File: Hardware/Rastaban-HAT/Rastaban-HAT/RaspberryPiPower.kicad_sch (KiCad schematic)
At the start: 13 parts, among them IC2 BCM53DS, Q3 DMG2305UX-7, U5 LM2596S-ADJ

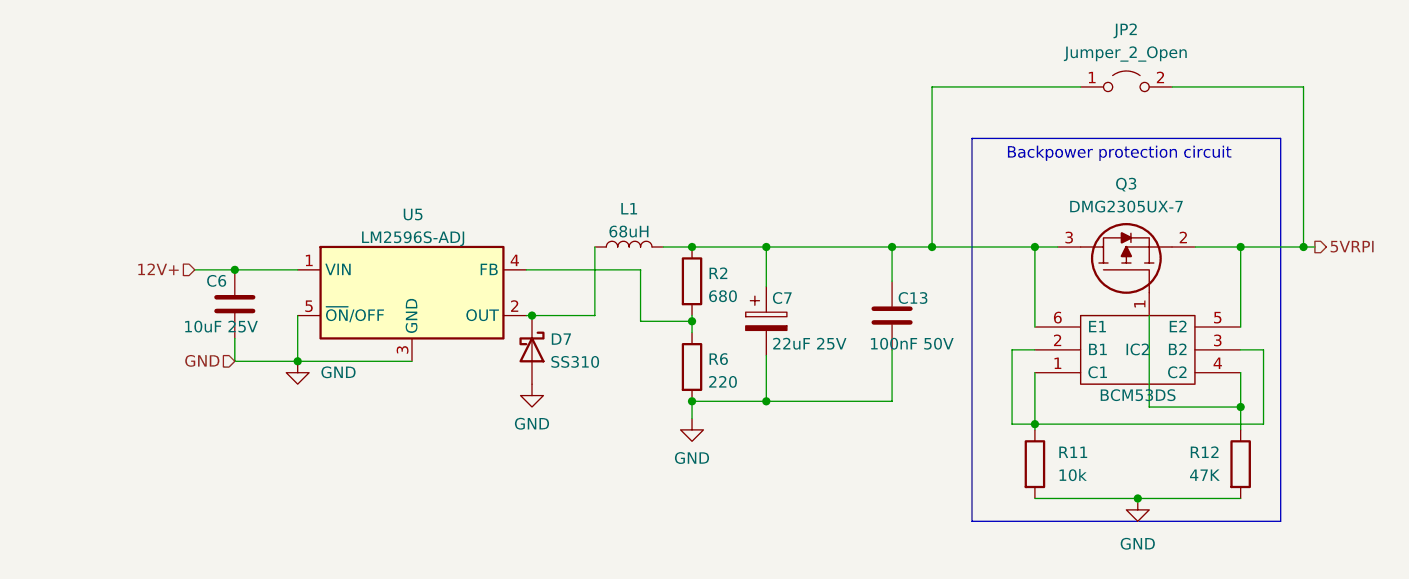
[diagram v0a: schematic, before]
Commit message: changed jumpers to 3.3V jumpers only
changed version numbers
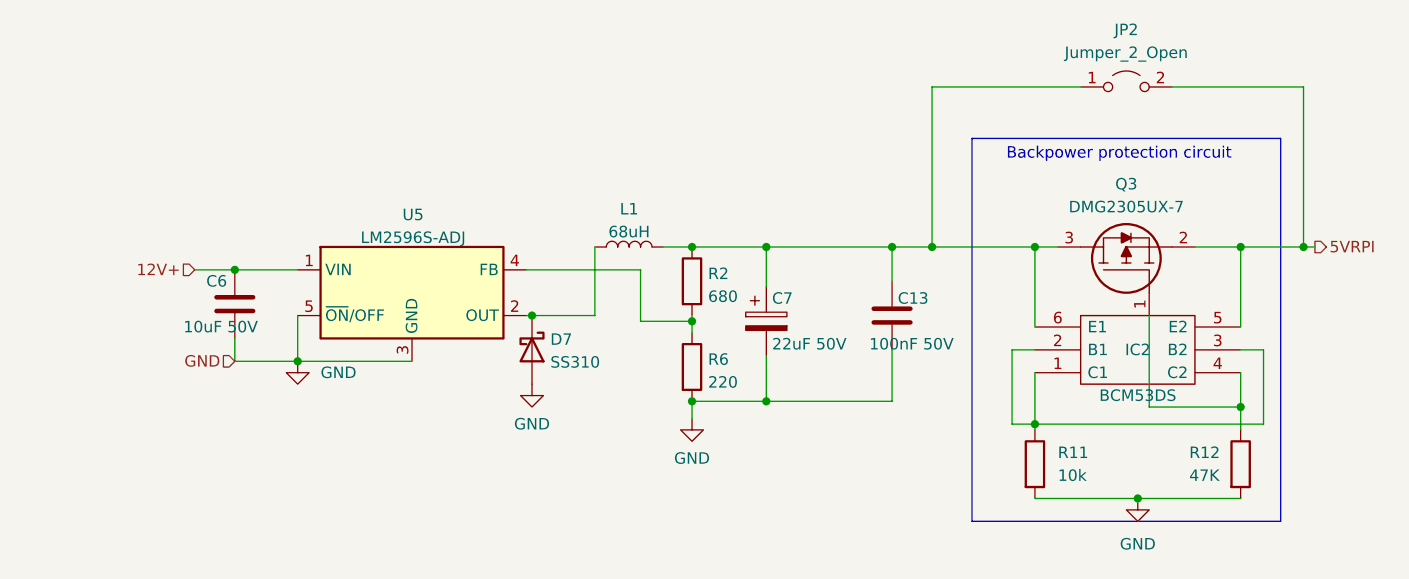
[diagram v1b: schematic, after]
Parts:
- C6: value 10uF 25V -> 10uF 50V
- C7: value 22uF 25V -> 22uF 50V
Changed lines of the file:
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@@
       (effects (font (size 1.27 1.27)) (justify left))
     )
-    (property "Value" "22uF 25V" (id 1) (at 109.855 69.215 0)
+    (property "Value" "22uF 50V" (id 1) (at 109.855 69.215 0)
       (effects (font (size 1.27 1.27)) (justify left))
     )
@@
       (effects (font (size 1.27 1.27)) (justify left))
     )
-    (property "Value" "10uF 25V" (id 1) (at 44.45 67.31 0)
+    (property "Value" "10uF 50V" (id 1) (at 44.45 67.31 0)
       (effects (font (size 1.27 1.27)) (justify left))
     )

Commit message: changed some component values in RPI power circuit
New components
-lm2596s -5.0
-ss510
Removed:
feedback resistors
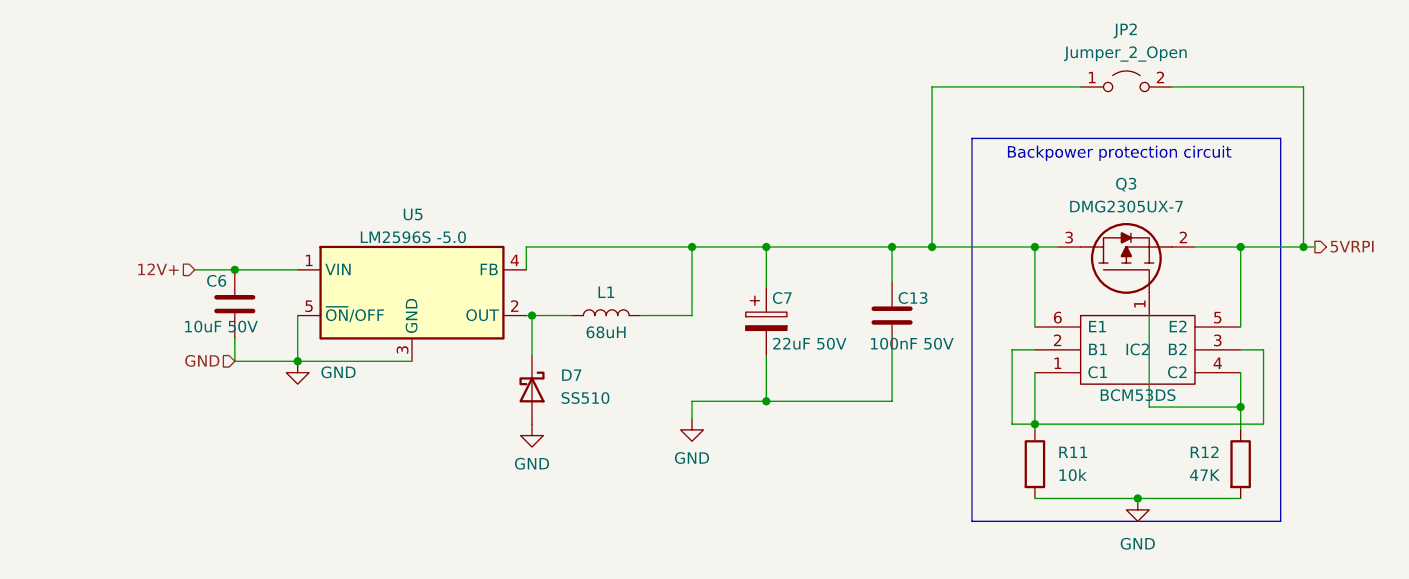
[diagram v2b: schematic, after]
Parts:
- removed R2: 680, Resistor_SMD:R_0805_2012Metric_Pad1.20x1.40mm_HandSolder, symbol Device:R
- removed R6: 220, Resistor_SMD:R_0805_2012Metric_Pad1.20x1.40mm_HandSolder, symbol Device:R
- D7: value SS310 -> SS510
- JP2: Purpose (none) -> Bypass Backpower protection circuit
- U5: value LM2596S-ADJ -> LM2596S -5.0; LCSC C347423 -> (none)
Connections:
- net at C13.2, C7.1, IC2.6 (E1)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: now also U5.4 (FB)
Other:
- moved on the sheet: D7, L1
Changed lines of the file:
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@@
   (title_block
     (title "Rastaban-HAT")
-    (date "2022-11-21")
-    (rev "1.4")
+    (date "2022-12-08")
+    (rev "1.5")
     (company "HAN")
     (comment 1 "Casper R. Tak")
@@
   (junction (at 50.165 60.96) (diameter 0) (color 0 0 0 0)
   )
+  (junction (at 100.965 58.42) (diameter 0) (color 0 0 0 0)
+  )
   (junction (at 139.065 58.42) (diameter 0) (color 0 0 0 0)
   )
-  (junction (at 100.965 75.565) (diameter 0) (color 0 0 0 0)
-  )
   (junction (at 161.925 58.42) (diameter 0) (color 0 0 0 0)
   )
@@
   (junction (at 139.065 78.105) (diameter 0) (color 0 0 0 0)
   )
-  (junction (at 100.965 58.42) (diameter 0) (color 0 0 0 0)
-  )
   (junction (at 127.635 58.42) (diameter 0) (color 0 0 0 0)
   )
-  (junction (at 100.965 66.675) (diameter 0) (color 0 0 0 0)
-  )
   (junction (at 83.185 66.04) (diameter 0) (color 0 0 0 0)
   )
@@
     (stroke (width 0) (type default) (color 0 0 0 0))
   )
+  (wire (pts (xy 83.185 70.485) (xy 83.185 66.04))
+    (stroke (width 0) (type default) (color 0 0 0 0))
+  )
   (wire (pts (xy 50.165 68.58) (xy 50.165 71.12))
     (stroke (width 0) (type default) (color 0 0 0 0))
@@
     (stroke (width 0) (type default) (color 0 0 0 0))
   )
-  (wire (pts (xy 97.79 58.42) (xy 100.965 58.42))
-    (stroke (width 0) (type default) (color 0 0 0 0))
-  )
   (wire (pts (xy 100.965 75.565) (xy 109.22 75.565))
     (stroke (width 0) (type default) (color 0 0 0 0))
   )
-  (wire (pts (xy 95.25 60.96) (xy 95.25 66.675))
+  (wire (pts (xy 82.55 58.42) (xy 100.965 58.42))
     (stroke (width 0) (type default) (color 0 0 0 0))
   )
@@
     (stroke (width 0) (type default) (color 0 0 0 0))
   )
-  (wire (pts (xy 82.55 60.96) (xy 95.25 60.96))
-    (stroke (width 0) (type default) (color 0 0 0 0))
-  )
   (wire (pts (xy 156.845 58.42) (xy 161.925 58.42))
     (stroke (width 0) (type default) (color 0 0 0 0))
@@
     (stroke (width 0) (type default) (color 0 0 0 0))
   )
-  (wire (pts (xy 90.17 66.04) (xy 90.17 58.42))
-    (stroke (width 0) (type default) (color 0 0 0 0))
-  )
   (wire (pts (xy 123.19 58.42) (xy 127.635 58.42))
     (stroke (width 0) (type default) (color 0 0 0 0))
@@
     (stroke (width 0) (type default) (color 0 0 0 0))
   )
-  (wire (pts (xy 100.965 66.675) (xy 100.965 67.945))
-    (stroke (width 0) (type default) (color 0 0 0 0))
-  )
   (wire (pts (xy 139.065 69.85) (xy 136.525 69.85))
     (stroke (width 0) (type default) (color 0 0 0 0))
@@
     (stroke (width 0) (type default) (color 0 0 0 0))
   )
+  (wire (pts (xy 95.25 66.04) (xy 100.965 66.04))
+    (stroke (width 0) (type default) (color 0 0 0 0))
+  )
   (wire (pts (xy 154.305 40.64) (xy 168.91 40.64))
     (stroke (width 0) (type default) (color 0 0 0 0))
@@
     (stroke (width 0) (type default) (color 0 0 0 0))
   )
-  (wire (pts (xy 100.965 66.04) (xy 100.965 66.675))
+  (wire (pts (xy 100.965 58.42) (xy 100.965 66.04))
     (stroke (width 0) (type default) (color 0 0 0 0))
   )
@@
     (stroke (width 0) (type default) (color 0 0 0 0))
   )
+  (wire (pts (xy 82.55 58.42) (xy 82.55 60.96))
+    (stroke (width 0) (type default) (color 0 0 0 0))
+  )
   (wire (pts (xy 161.925 72.39) (xy 161.925 76.2))
     (stroke (width 0) (type default) (color 0 0 0 0))
@@
     (stroke (width 0) (type default) (color 0 0 0 0))
   )
-  (wire (pts (xy 95.25 66.675) (xy 100.965 66.675))
-    (stroke (width 0) (type default) (color 0 0 0 0))
-  )
   (wire (pts (xy 139.065 58.42) (xy 141.605 58.42))
     (stroke (width 0) (type default) (color 0 0 0 0))
@@
     (stroke (width 0) (type default) (color 0 0 0 0))
   )
-  (wire (pts (xy 83.185 66.04) (xy 90.17 66.04))
+  (wire (pts (xy 83.185 66.04) (xy 87.63 66.04))
     (stroke (width 0) (type default) (color 0 0 0 0))
   )
@@
     (pin "2")
   )
-  (symbol (lib_id "power:GND") (at 83.185 73.66 0) (unit 1)
-    (in_bom yes) (on_board yes) (fields_autoplaced)
-    (property "Reference" "#PWR0105" (id 0) (at 83.185 80.01 0)
-      (effects (font (size 1.27 1.27)) hide)
-    )
-    (property "Value" "GND" (id 1) (at 83.185 78.1034 0))
-    (property "Footprint" "" (id 2) (at 83.185 73.66 0)
-      (effects (font (size 1.27 1.27)) hide)
-    )
-    (property "Datasheet" "" (id 3) (at 83.185 73.66 0)
+  (symbol (lib_id "power:GND") (at 83.185 78.105 0) (unit 1)
+    (in_bom yes) (on_board yes) (fields_autoplaced)
+    (property "Reference" "#PWR0105" (id 0) (at 83.185 84.455 0)
+      (effects (font (size 1.27 1.27)) hide)
+    )
+    (property "Value" "GND" (id 1) (at 83.185 82.5484 0))
+    (property "Footprint" "" (id 2) (at 83.185 78.105 0)
+      (effects (font (size 1.27 1.27)) hide)
+    )
+    (property "Datasheet" "" (id 3) (at 83.185 78.105 0)
       (effects (font (size 1.27 1.27)) hide)
     )
@@
       (effects (font (size 1.27 1.27)) hide)
     )
+    (property "Purpose" "Bypass Backpower protection circuit" (id 4) (at 149.225 40.64 0)
+      (effects (font (size 1.27 1.27)) hide)
+    )
     (pin "1")
     (pin "2")
@@
     (pin "1")
   )
-  (symbol (lib_id "Device:D_Schottky") (at 83.185 69.85 270) (unit 1)
-    (in_bom yes) (on_board yes) (fields_autoplaced)
-    (property "Reference" "D7" (id 0) (at 85.217 68.6978 90)
-      (effects (font (size 1.27 1.27)) (justify left))
-    )
-    (property "Value" "SS310" (id 1) (at 85.217 71.2347 90)
-      (effects (font (size 1.27 1.27)) (justify left))
-    )
-    (property "Footprint" "SamacSys_Parts:SOD2512X110N" (id 2) (at 83.185 69.85 0)
-      (effects (font (size 1.27 1.27)) hide)
-    )
-    (property "Datasheet" "~" (id 3) (at 83.185 69.85 0)
+  (symbol (lib_id "Device:D_Schottky") (at 83.185 74.295 270) (unit 1)
+    (in_bom yes) (on_board yes) (fields_autoplaced)
+    (property "Reference" "D7" (id 0) (at 86.36 72.7074 90)
+      (effects (font (size 1.27 1.27)) (justify left))
+    )
+    (property "Value" "SS510" (id 1) (at 86.36 75.2474 90)
+      (effects (font (size 1.27 1.27)) (justify left))
+    )
+    (property "Footprint" "SamacSys_Parts:SOD2512X110N" (id 2) (at 83.185 74.295 0)
+      (effects (font (size 1.27 1.27)) hide)
+    )
+    (property "Datasheet" "~" (id 3) (at 83.185 74.295 0)
       (effects (font (size 1.27 1.27)) hide)
     )
@@
     (in_bom yes) (on_board yes)
     (property "Reference" "U5" (id 0) (at 69.977 54.8472 0))
-    (property "Value" "LM2596S-ADJ" (id 1) (at 69.977 57.3841 0))
+    (property "Value" "LM2596S -5.0" (id 1) (at 69.977 57.3841 0))
     (property "Footprint" "Package_TO_SOT_SMD:TO-263-5_TabPin3" (id 2) (at 71.12 69.85 0)
       (effects (font (size 1.27 1.27) italic) (justify left) hide)
@@
       (effects (font (size 1.27 1.27)) hide)
     )
-    (property "LCSC" "C347423" (id 5) (at 69.85 63.5 0)
+    (property "LCSC" "" (id 5) (at 69.85 63.5 0)
       (effects (font (size 1.27 1.27)) hide)
     )
@@
     (pin "5")
   )
-  (symbol (lib_id "Device:L") (at 93.98 58.42 90) (unit 1)
-    (in_bom yes) (on_board yes) (fields_autoplaced)
-    (property "Reference" "L1" (id 0) (at 93.98 54.2122 90))
-    (property "Value" "68uH" (id 1) (at 93.98 56.7491 90))
-    (property "Footprint" "Inductor_SMD:L_Bourns-SRU8028_8.0x8.0mm" (id 2) (at 93.98 58.42 0)
-      (effects (font (size 1.27 1.27)) hide)
-    )
-    (property "Datasheet" "~" (id 3) (at 93.98 58.42 0)
-      (effects (font (size 1.27 1.27)) hide)
-    )
-    (property "LCSC" "C82571" (id 5) (at 93.98 58.42 90)
+  (symbol (lib_id "Device:L") (at 91.44 66.04 90) (unit 1)
+    (in_bom yes) (on_board yes)
+    (property "Reference" "L1" (id 0) (at 91.44 63.5 90))
+    (property "Value" "68uH" (id 1) (at 91.44 67.945 90))
+    (property "Footprint" "Inductor_SMD:L_Bourns-SRU8028_8.0x8.0mm" (id 2) (at 91.44 66.04 0)
+      (effects (font (size 1.27 1.27)) hide)
+    )
+    (property "Datasheet" "~" (id 3) (at 91.44 66.04 0)
+      (effects (font (size 1.27 1.27)) hide)
+    )
+    (property "LCSC" "C82571" (id 5) (at 91.44 66.04 90)
       (effects (font (size 1.27 1.27)) hide)
     )
@@
     (pin "6")
   )
-  (symbol (lib_id "Device:R") (at 100.965 71.755 0) (unit 1)
-    (in_bom yes) (on_board yes) (fields_autoplaced)
-    (property "Reference" "R6" (id 0) (at 102.743 70.9203 0)
-      (effects (font (size 1.27 1.27)) (justify left))
-    )
-    (property "Value" "220" (id 1) (at 102.743 73.4572 0)
-      (effects (font (size 1.27 1.27)) (justify left))
-    )
-    (property "Footprint" "Resistor_SMD:R_0805_2012Metric_Pad1.20x1.40mm_HandSolder" (id 2) (at 99.187 71.755 90)
-      (effects (font (size 1.27 1.27)) hide)
-    )
-    (property "Datasheet" "~" (id 3) (at 100.965 71.755 0)
-      (effects (font (size 1.27 1.27)) hide)
-    )
-    (property "LCSC" "C17557" (id 5) (at 100.965 71.755 0)
-      (effects (font (size 1.27 1.27)) hide)
-    )
-    (pin "1")
-    (pin "2")
-  )
-  (symbol (lib_id "Device:R") (at 100.965 62.23 0) (unit 1)
-    (in_bom yes) (on_board yes) (fields_autoplaced)
-    (property "Reference" "R2" (id 0) (at 102.743 61.3953 0)
-      (effects (font (size 1.27 1.27)) (justify left))
-    )
-    (property "Value" "680" (id 1) (at 102.743 63.9322 0)
-      (effects (font (size 1.27 1.27)) (justify left))
-    )
-    (property "Footprint" "Resistor_SMD:R_0805_2012Metric_Pad1.20x1.40mm_HandSolder" (id 2) (at 99.187 62.23 90)
-      (effects (font (size 1.27 1.27)) hide)
-    )
-    (property "Datasheet" "~" (id 3) (at 100.965 62.23 0)
-      (effects (font (size 1.27 1.27)) hide)
-    )
-    (property "LCSC" "C17798" (id 5) (at 100.965 62.23 0)
-      (effects (font (size 1.27 1.27)) hide)
-    )
-    (pin "1")
-    (pin "2")
-  )
 )

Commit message: changed capacitor types/values
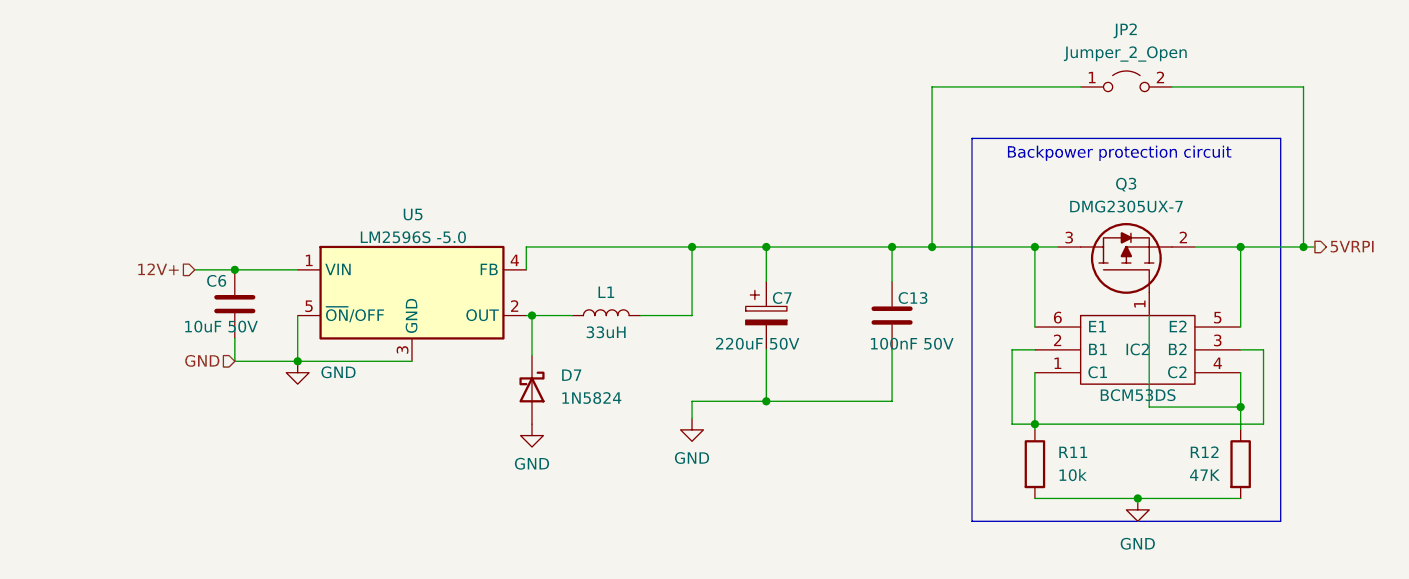
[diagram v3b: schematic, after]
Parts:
- C13: footprint Capacitor_SMD:C_0805_2012Metric_Pad1.18x1.45mm_HandSolder -> Capacitor_SMD:C_1206_3216Metric_Pad1.33x1.80mm_HandSolder
- C7: value 22uF 50V -> 220uF 50V; footprint Capacitor_SMD:C_0805_2012Metric_Pad1.18x1.45mm_HandSolder -> Capacitor_SMD:CP_Elec_8x10; LCSC C5155340 -> C445063; Manufacturer_Part_Number (none) -> C3339; Purpose (none) -> decoupling
- D7: value SS510 -> 1N5824
- L1: value 68uH -> 33uH
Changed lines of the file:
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@@
     (stroke (width 0) (type default) (color 0 0 0 0))
   )
-  (wire (pts (xy 109.22 62.865) (xy 109.22 58.42))
+  (wire (pts (xy 109.22 62.23) (xy 109.22 58.42))
     (stroke (width 0) (type default) (color 0 0 0 0))
   )
@@
     (stroke (width 0) (type default) (color 0 0 0 0))
   )
-  (wire (pts (xy 109.22 70.485) (xy 109.22 75.565))
+  (wire (pts (xy 109.22 69.85) (xy 109.22 75.565))
     (stroke (width 0) (type default) (color 0 0 0 0))
   )
@@
   (hierarchical_label "GND" (shape input) (at 50.165 71.12 180)
     (effects (font (size 1.27 1.27)) (justify right))
-  )
-  (symbol (lib_id "Device:C_Polarized") (at 109.22 66.675 0) (unit 1)
-    (in_bom yes) (on_board yes)
-    (property "Reference" "C7" (id 0) (at 109.855 64.135 0)
-      (effects (font (size 1.27 1.27)) (justify left))
-    )
-    (property "Value" "22uF 50V" (id 1) (at 109.855 69.215 0)
-      (effects (font (size 1.27 1.27)) (justify left))
-    )
-    (property "Footprint" "Capacitor_SMD:C_0805_2012Metric_Pad1.18x1.45mm_HandSolder" (id 2) (at 110.1852 70.485 0)
-      (effects (font (size 1.27 1.27)) hide)
-    )
-    (property "Datasheet" "~" (id 3) (at 109.22 66.675 0)
-      (effects (font (size 1.27 1.27)) hide)
-    )
-    (property "LCSC" "C5155340" (id 5) (at 109.22 66.675 0)
-      (effects (font (size 1.27 1.27)) hide)
-    )
-    (pin "1")
-    (pin "2")
   )
   (symbol (lib_id "power:GND") (at 83.185 78.105 0) (unit 1)
@@
     (pin "3")
   )
+  (symbol (lib_id "Device:C_Polarized") (at 109.22 66.04 0) (unit 1)
+    (in_bom yes) (on_board yes)
+    (property "Reference" "C7" (id 0) (at 109.855 64.135 0)
+      (effects (font (size 1.27 1.27)) (justify left))
+    )
+    (property "Value" "220uF 50V" (id 1) (at 103.505 69.215 0)
+      (effects (font (size 1.27 1.27)) (justify left))
+    )
+    (property "Footprint" "Capacitor_SMD:CP_Elec_8x10" (id 2) (at 110.1852 69.85 0)
+      (effects (font (size 1.27 1.27)) hide)
+    )
+    (property "Datasheet" "~" (id 3) (at 109.22 66.04 0)
+      (effects (font (size 1.27 1.27)) hide)
+    )
+    (property "LCSC Part#" "" (id 4) (at 109.22 66.04 0)
+      (effects (font (size 1.27 1.27)) hide)
+    )
+    (property "Manufacturer_Part_Number" "C3339" (id 5) (at 109.22 66.04 0)
+      (effects (font (size 1.27 1.27)) hide)
+    )
+    (property "Purpose" "decoupling" (id 6) (at 109.22 66.04 0)
+      (effects (font (size 1.27 1.27)) hide)
+    )
+    (property "LCSC" "C445063" (id 7) (at 109.22 66.04 0)
+      (effects (font (size 1.27 1.27)) hide)
+    )
+    (pin "1")
+    (pin "2")
+  )
   (symbol (lib_id "Device:R") (at 139.065 82.55 0) (unit 1)
     (in_bom yes) (on_board yes) (fields_autoplaced)
@@
       (effects (font (size 1.27 1.27)) (justify right))
     )
-    (property "Footprint" "Capacitor_SMD:C_0805_2012Metric_Pad1.18x1.45mm_HandSolder" (id 2) (at 122.2248 62.23 0)
+    (property "Footprint" "Capacitor_SMD:C_1206_3216Metric_Pad1.33x1.80mm_HandSolder" (id 2) (at 122.2248 62.23 0)
       (effects (font (size 1.27 1.27)) hide)
     )
@@
       (effects (font (size 1.27 1.27)) (justify left))
     )
-    (property "Value" "SS510" (id 1) (at 86.36 75.2474 90)
+    (property "Value" "1N5824" (id 1) (at 86.36 75.2474 90)
       (effects (font (size 1.27 1.27)) (justify left))
     )
@@
     (in_bom yes) (on_board yes)
     (property "Reference" "L1" (id 0) (at 91.44 63.5 90))
-    (property "Value" "68uH" (id 1) (at 91.44 67.945 90))
+    (property "Value" "33uH" (id 1) (at 91.44 67.945 90))
     (property "Footprint" "Inductor_SMD:L_Bourns-SRU8028_8.0x8.0mm" (id 2) (at 91.44 66.04 0)
       (effects (font (size 1.27 1.27)) hide)
